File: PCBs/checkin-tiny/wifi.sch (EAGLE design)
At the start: 23 parts, among them IC1 Primary, IC2 Display, Q1 12 MHz, Q2 12 MHz

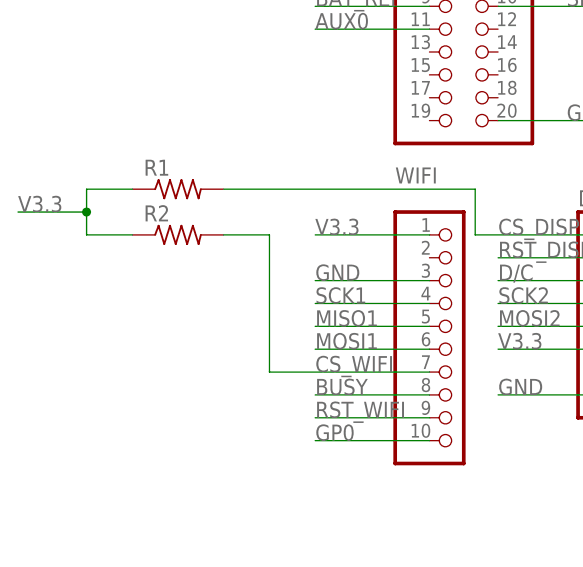
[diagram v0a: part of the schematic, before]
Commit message: Fix resistor labels on Wi-Fi board
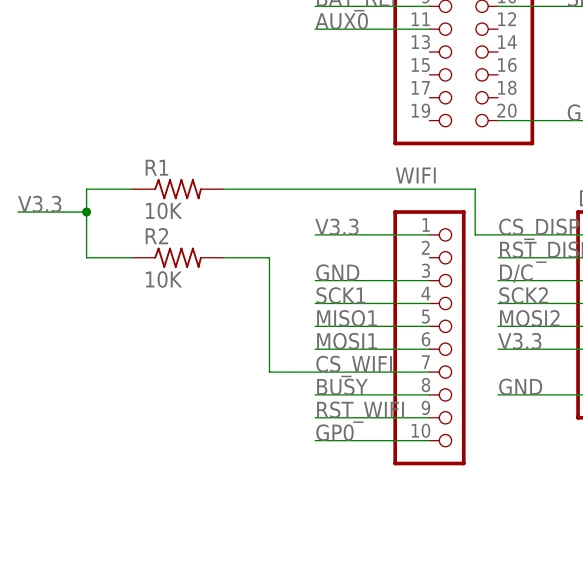
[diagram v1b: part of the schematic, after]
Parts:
- R1, R2: value (none) -> 10K
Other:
- moved on the sheet: R2
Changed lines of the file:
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@@
 <?xml version="1.0" encoding="utf-8"?>
 <!DOCTYPE eagle SYSTEM "eagle.dtd">
-<eagle version="9.4.2">
+<eagle version="9.5.2">
 <drawing>
 <settings>
@@
 <part name="C3" library="rcl" library_urn="urn:adsk.eagle:library:334" deviceset="C-EU" device="C1206" package3d_urn="urn:adsk.eagle:package:23618/2" value="16pF"/>
 <part name="Q1" library="adafruit" library_urn="urn:adsk.eagle:library:420" deviceset="CRYSTAL" device="HC49S" package3d_urn="urn:adsk.eagle:package:6240901/1" value="12 MHz"/>
-<part name="R1" library="rcl" library_urn="urn:adsk.eagle:library:334" deviceset="R-US_" device="R1206" package3d_urn="urn:adsk.eagle:package:23540/2"/>
-<part name="R2" library="rcl" library_urn="urn:adsk.eagle:library:334" deviceset="R-US_" device="R1206" package3d_urn="urn:adsk.eagle:package:23540/2"/>
+<part name="R1" library="rcl" library_urn="urn:adsk.eagle:library:334" deviceset="R-US_" device="R1206" package3d_urn="urn:adsk.eagle:package:23540/2" value="10K"/>
+<part name="R2" library="rcl" library_urn="urn:adsk.eagle:library:334" deviceset="R-US_" device="R1206" package3d_urn="urn:adsk.eagle:package:23540/2" value="10K"/>
 <part name="C4" library="rcl" library_urn="urn:adsk.eagle:library:334" deviceset="C-EU" device="C1206" package3d_urn="urn:adsk.eagle:package:23618/2" value="0.1uF"/>
 <part name="C5" library="rcl" library_urn="urn:adsk.eagle:library:334" deviceset="C-EU" device="C1206" package3d_urn="urn:adsk.eagle:package:23618/2" value="16pF"/>
@@
 <attribute name="VALUE" x="-26.67" y="47.498" size="1.778" layer="96"/>
 </instance>
-<instance part="R2" gate="G$1" x="-22.86" y="45.72" smashed="yes">
-<attribute name="NAME" x="-26.67" y="47.2186" size="1.778" layer="95"/>
-<attribute name="VALUE" x="-26.67" y="42.418" size="1.778" layer="96"/>
+<instance part="R2" gate="G$1" x="-22.86" y="43.18" smashed="yes">
+<attribute name="NAME" x="-26.67" y="44.6786" size="1.778" layer="95"/>
+<attribute name="VALUE" x="-26.67" y="39.878" size="1.778" layer="96"/>
 </instance>
 <instance part="C4" gate="G$1" x="132.08" y="66.04" smashed="yes">
@@
 <wire x1="-33.02" y1="50.8" x2="-33.02" y2="48.26" width="0.1524" layer="91"/>
 <pinref part="R2" gate="G$1" pin="1"/>
-<wire x1="-33.02" y1="48.26" x2="-33.02" y2="45.72" width="0.1524" layer="91"/>
-<wire x1="-33.02" y1="45.72" x2="-27.94" y2="45.72" width="0.1524" layer="91"/>
+<wire x1="-33.02" y1="48.26" x2="-33.02" y2="43.18" width="0.1524" layer="91"/>
+<wire x1="-33.02" y1="43.18" x2="-27.94" y2="43.18" width="0.1524" layer="91"/>
 <wire x1="-33.02" y1="48.26" x2="-40.64" y2="48.26" width="0.1524" layer="91"/>
 <junction x="-33.02" y="48.26"/>
@@
 <wire x1="5.08" y1="30.48" x2="-12.7" y2="30.48" width="0.1524" layer="91"/>
 <label x="-7.62" y="30.48" size="1.778" layer="95"/>
-<wire x1="-12.7" y1="30.48" x2="-12.7" y2="45.72" width="0.1524" layer="91"/>
+<wire x1="-12.7" y1="30.48" x2="-12.7" y2="43.18" width="0.1524" layer="91"/>
 <pinref part="R2" gate="G$1" pin="2"/>
-<wire x1="-12.7" y1="45.72" x2="-17.78" y2="45.72" width="0.1524" layer="91"/>
-</segment>
-<segment>
+<wire x1="-12.7" y1="43.18" x2="-17.78" y2="43.18" width="0.1524" layer="91"/>
+</segment>
+<segment>
